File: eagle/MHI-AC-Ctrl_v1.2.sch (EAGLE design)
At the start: 15 parts, among them U1 TSR_1-2450

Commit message: - refactored board
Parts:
- removed TP6, TP7, TP8: TPPAD1-13, testpad:TPPAD1-13
- added R1: 4.7K, rcl:R-EU_0204/7
- added U2: DS18B20, DS18B20:DS18B20
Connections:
- net MISO_LV renamed N$1
- net MOSI_LV renamed N$2
- net +5V: now also R1.2, U2.VDD; no longer TP8.TP
- net GND: now also U2.GND; no longer TP7.TP
- net N$14: now also R1.1, U2.DQ; no longer TP6.TP
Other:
- note added: "Optional: DS18B20"
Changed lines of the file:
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@@
 <part name="P+2" library="supply1" library_urn="urn:adsk.eagle:library:371" deviceset="+5V" device=""/>
 <part name="P+3" library="supply1" library_urn="urn:adsk.eagle:library:371" deviceset="+12V" device=""/>
-<part name="GND5" library="supply1" library_urn="urn:adsk.eagle:library:371" deviceset="GND" device=""/>
 <part name="U$4" library="srg" deviceset="JST-PH_5-PIN_HEADER" device=""/>
 <part name="C2" library="rcl" library_urn="urn:adsk.eagle:library:334" deviceset="C-EU" device="025-024X044" package3d_urn="urn:adsk.eagle:package:23630/1" value="100n"/>
@@
 <part name="P+6" library="supply1" library_urn="urn:adsk.eagle:library:371" deviceset="+5V" device=""/>
 <part name="P+4" library="supply1" library_urn="urn:adsk.eagle:library:371" deviceset="+12V" device=""/>
-<part name="TP6" library="testpad" library_urn="urn:adsk.eagle:library:385" deviceset="TP" device="PAD1-13" package3d_urn="urn:adsk.eagle:package:27946/1"/>
-<part name="TP7" library="testpad" library_urn="urn:adsk.eagle:library:385" deviceset="TP" device="PAD1-13" package3d_urn="urn:adsk.eagle:package:27946/1"/>
-<part name="TP8" library="testpad" library_urn="urn:adsk.eagle:library:385" deviceset="TP" device="PAD1-13" package3d_urn="urn:adsk.eagle:package:27946/1"/>
-<part name="P+5" library="supply1" library_urn="urn:adsk.eagle:library:371" deviceset="+5V" device=""/>
 <part name="TP9" library="testpad" library_urn="urn:adsk.eagle:library:385" deviceset="TP" device="PAD1-13" package3d_urn="urn:adsk.eagle:package:27946/1"/>
 <part name="TP10" library="testpad" library_urn="urn:adsk.eagle:library:385" deviceset="TP" device="PAD1-13" package3d_urn="urn:adsk.eagle:package:27946/1"/>
@@
 <part name="TP12" library="testpad" library_urn="urn:adsk.eagle:library:385" deviceset="TP" device="PAD1-13" package3d_urn="urn:adsk.eagle:package:27946/1"/>
 <part name="TP13" library="testpad" library_urn="urn:adsk.eagle:library:385" deviceset="TP" device="PAD1-13" package3d_urn="urn:adsk.eagle:package:27946/1"/>
+<part name="R1" library="rcl" library_urn="urn:adsk.eagle:library:334" deviceset="R-EU_" device="0204/7" package3d_urn="urn:adsk.eagle:package:23498/2" value="4.7K"/>
+<part name="U2" library="DS18B20" deviceset="DS18B20" device=""/>
 </parts>
 <sheets>
 <sheet>
 <plain>
+<circle x="35.56" y="83.82" radius="23.417640625" width="0.1524" layer="94"/>
+<text x="25.4" y="101.6" size="1.778" layer="94">Optional: DS18B20</text>
 </plain>
 <instances>
@@
 <attribute name="VALUE" x="-27.94" y="76.2" size="1.778" layer="96"/>
 </instance>
-<instance part="GND5" gate="1" x="-30.48" y="30.48" smashed="yes">
-<attribute name="VALUE" x="-33.02" y="27.94" size="1.778" layer="96"/>
-</instance>
 <instance part="U$4" gate="G$1" x="-86.36" y="38.1" smashed="yes" rot="R180"/>
 <instance part="C2" gate="G$1" x="55.88" y="25.4" smashed="yes">
@@
 <attribute name="VALUE" x="11.684" y="61.341" size="1.778" layer="96"/>
 </instance>
-<instance part="GND9" gate="1" x="10.16" y="30.48" smashed="yes">
-<attribute name="VALUE" x="7.62" y="27.94" size="1.778" layer="96"/>
+<instance part="GND9" gate="1" x="-10.16" y="25.4" smashed="yes">
+<attribute name="VALUE" x="-12.7" y="22.86" size="1.778" layer="96"/>
 </instance>
 <instance part="LS1" gate="G$1" x="-10.16" y="43.18" smashed="yes" rot="MR0">
@@
 <attribute name="VALUE" x="-40.64" y="29.21" size="1.778" layer="96"/>
 </instance>
-<instance part="TP6" gate="G$1" x="60.96" y="35.56" smashed="yes" rot="R270">
-<attribute name="TP_SIGNAL_NAME" x="59.69" y="34.29" size="1.778" layer="97" rot="R270"/>
-</instance>
-<instance part="TP7" gate="G$1" x="68.58" y="36.83" smashed="yes">
-<attribute name="TP_SIGNAL_NAME" x="69.85" y="35.56" size="1.778" layer="97"/>
-</instance>
-<instance part="TP8" gate="G$1" x="68.58" y="45.72" smashed="yes" rot="R180">
-<attribute name="TP_SIGNAL_NAME" x="67.31" y="46.99" size="1.778" layer="97" rot="R180"/>
-</instance>
-<instance part="P+5" gate="1" x="68.58" y="52.07" smashed="yes">
-<attribute name="VALUE" x="71.12" y="54.61" size="1.778" layer="96" rot="R180"/>
-</instance>
 <instance part="TP9" gate="G$1" x="-55.88" y="49.53" smashed="yes">
 <attribute name="TP_SIGNAL_NAME" x="-54.61" y="48.26" size="1.778" layer="97"/>
@@
 <instance part="TP13" gate="G$1" x="-66.04" y="49.53" smashed="yes">
 <attribute name="TP_SIGNAL_NAME" x="-64.77" y="48.26" size="1.778" layer="97"/>
+</instance>
+<instance part="R1" gate="G$1" x="35.56" y="68.58" smashed="yes" rot="MR0">
+<attribute name="NAME" x="34.29" y="70.0786" size="1.778" layer="95" rot="MR0"/>
+<attribute name="VALUE" x="36.83" y="65.278" size="1.778" layer="96" rot="MR0"/>
+</instance>
+<instance part="U2" gate="G$1" x="35.56" y="88.9" smashed="yes" rot="MR0">
+<attribute name="NAME" x="43.194490625" y="96.78896875" size="1.78138125" layer="95" rot="MR0"/>
+<attribute name="VALUE" x="43.183340625" y="81.02255" size="1.77878125" layer="96" rot="MR0" align="top-left"/>
 </instance>
 </instances>
@@
 <pinref part="GND2" gate="1" pin="GND"/>
 <wire x1="55.88" y1="33.02" x2="68.58" y2="33.02" width="0.1524" layer="91"/>
-<pinref part="TP7" gate="G$1" pin="TP"/>
-<wire x1="68.58" y1="33.02" x2="68.58" y2="34.29" width="0.1524" layer="91"/>
-<junction x="68.58" y="33.02"/>
 </segment>
 <segment>
@@
 <wire x1="-78.74" y1="43.18" x2="-55.88" y2="43.18" width="0.1524" layer="91"/>
 <wire x1="-55.88" y1="43.18" x2="-30.48" y2="43.18" width="0.1524" layer="91"/>
-<pinref part="GND5" gate="1" pin="GND"/>
 <pinref part="LS1" gate="G$1" pin="GND.2"/>
-<wire x1="-30.48" y1="33.02" x2="-30.48" y2="40.64" width="0.1524" layer="91"/>
+<wire x1="-30.48" y1="27.94" x2="-30.48" y2="40.64" width="0.1524" layer="91"/>
 <wire x1="-30.48" y1="40.64" x2="-25.4" y2="40.64" width="0.1524" layer="91"/>
 <wire x1="-30.48" y1="43.18" x2="-30.48" y2="40.64" width="0.1524" layer="91"/>
@@
 <wire x1="-55.88" y1="43.18" x2="-55.88" y2="46.99" width="0.1524" layer="91"/>
 <junction x="-55.88" y="43.18"/>
+<pinref part="GND9" gate="1" pin="GND"/>
+<wire x1="7.62" y1="27.94" x2="-10.16" y2="27.94" width="0.1524" layer="91"/>
+<wire x1="-30.48" y1="27.94" x2="-10.16" y2="27.94" width="0.1524" layer="91"/>
+<junction x="-10.16" y="27.94"/>
+<pinref part="LS1" gate="G$1" pin="GND.1"/>
+<wire x1="5.08" y1="40.64" x2="7.62" y2="40.64" width="0.1524" layer="91"/>
+<wire x1="7.62" y1="40.64" x2="7.62" y2="27.94" width="0.1524" layer="91"/>
 </segment>
 <segment>
@@
 <junction x="-10.16" y="60.96"/>
 <wire x1="10.16" y1="60.96" x2="-10.16" y2="60.96" width="0.1524" layer="91"/>
-</segment>
-<segment>
-<pinref part="LS1" gate="G$1" pin="GND.1"/>
-<pinref part="GND9" gate="1" pin="GND"/>
-<wire x1="5.08" y1="40.64" x2="10.16" y2="40.64" width="0.1524" layer="91"/>
-<wire x1="10.16" y1="40.64" x2="10.16" y2="33.02" width="0.1524" layer="91"/>
+<pinref part="U2" gate="G$1" pin="GND"/>
+<wire x1="25.4" y1="83.82" x2="25.4" y2="60.96" width="0.1524" layer="91"/>
+<wire x1="25.4" y1="60.96" x2="10.16" y2="60.96" width="0.1524" layer="91"/>
+<junction x="10.16" y="60.96"/>
 </segment>
 </net>
@@
 <wire x1="0" y1="68.58" x2="10.16" y2="68.58" width="0.1524" layer="91"/>
 <junction x="10.16" y="68.58"/>
+<wire x1="10.16" y1="68.58" x2="20.32" y2="68.58" width="0.1524" layer="91"/>
+<wire x1="20.32" y1="68.58" x2="20.32" y2="93.98" width="0.1524" layer="91"/>
+<pinref part="U2" gate="G$1" pin="VDD"/>
+<wire x1="20.32" y1="93.98" x2="25.4" y2="93.98" width="0.1524" layer="91"/>
+<pinref part="R1" gate="G$1" pin="2"/>
+<wire x1="20.32" y1="68.58" x2="30.48" y2="68.58" width="0.1524" layer="91"/>
+<junction x="20.32" y="68.58"/>
 </segment>
 <segment>
@@
 <pinref part="LS1" gate="G$1" pin="HV"/>
 <wire x1="-27.94" y1="43.18" x2="-25.4" y2="43.18" width="0.1524" layer="91"/>
-</segment>
-<segment>
-<pinref part="P+5" gate="1" pin="+5V"/>
-<pinref part="TP8" gate="G$1" pin="TP"/>
-<wire x1="68.58" y1="49.53" x2="68.58" y2="48.26" width="0.1524" layer="91"/>
 </segment>
 </net>
@@
 </segment>
 </net>
-<net name="MOSI_LV" class="0">
-<segment>
-<pinref part="U$1" gate="G$1" pin="D7"/>
-<pinref part="LS1" gate="G$1" pin="LV4"/>
-<wire x1="20.32" y1="35.56" x2="5.08" y2="35.56" width="0.1524" layer="91"/>
-</segment>
-</net>
-<net name="MISO_LV" class="0">
-<segment>
-<pinref part="U$1" gate="G$1" pin="D6"/>
-<pinref part="LS1" gate="G$1" pin="LV3"/>
-<wire x1="20.32" y1="38.1" x2="5.08" y2="38.1" width="0.1524" layer="91"/>
-</segment>
-</net>
 <net name="SCL_LV" class="0">
 <segment>
@@
 <segment>
 <pinref part="U$1" gate="G$1" pin="D4"/>
-<pinref part="TP6" gate="G$1" pin="TP"/>
 <wire x1="55.88" y1="35.56" x2="58.42" y2="35.56" width="0.1524" layer="91"/>
-</segment>
-</net>
+<wire x1="58.42" y1="35.56" x2="58.42" y2="68.58" width="0.1524" layer="91"/>
+<pinref part="U2" gate="G$1" pin="DQ"/>
+<pinref part="R1" gate="G$1" pin="1"/>
+<wire x1="45.72" y1="68.58" x2="45.72" y2="88.9" width="0.1524" layer="91"/>
+<wire x1="40.64" y1="68.58" x2="45.72" y2="68.58" width="0.1524" layer="91"/>
+<junction x="45.72" y="68.58"/>
+<wire x1="45.72" y1="68.58" x2="58.42" y2="68.58" width="0.1524" layer="91"/>
+</segment>
+</net>
+<net name="N$1" class="0">
+<segment>
+<pinref part="LS1" gate="G$1" pin="LV3"/>
+<pinref part="U$1" gate="G$1" pin="D6"/>
+<wire x1="5.08" y1="38.1" x2="20.32" y2="38.1" width="0.1524" layer="91"/>
+</segment>
+</net>
+<net name="N$2" class="0">
+<segment>
+<pinref part="LS1" gate="G$1" pin="LV4"/>
+<pinref part="U$1" gate="G$1" pin="D7"/>
+<wire x1="5.08" y1="35.56" x2="20.32" y2="35.56" width="0.1524" layer="91"/>
+</segment>
+</net>

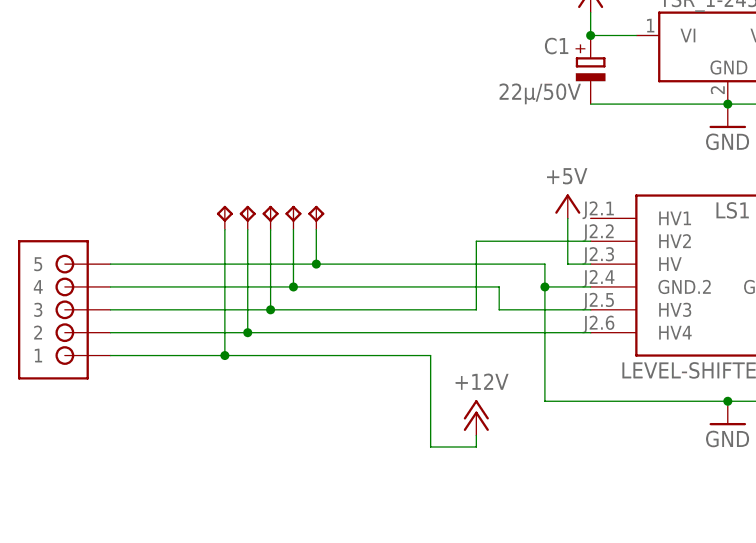
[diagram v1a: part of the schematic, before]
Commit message: invert pin 2 and 3, remove AIRWIRE from DS18x20
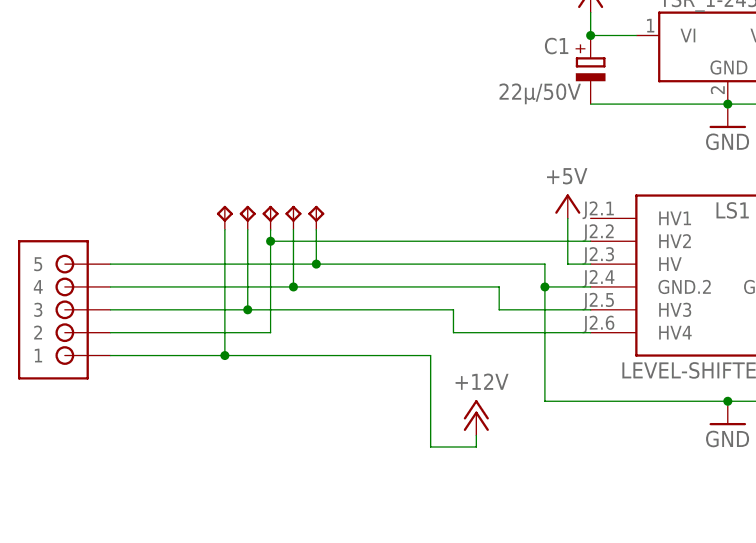
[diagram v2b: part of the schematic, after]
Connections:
- removed net MOSI: LS1.HV4, TP12.TP, U$4.2
- removed net SCL: LS1.HV2, TP11.TP, U$4.3
- new net N$3: LS1.HV2, TP11.TP, U$4.2
- new net N$4: LS1.HV4, TP12.TP, U$4.3
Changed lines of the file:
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@@
-</segment>
-</net>
-<net name="MOSI" class="0">
-<segment>
-<wire x1="-25.4" y1="35.56" x2="-63.5" y2="35.56" width="0.1524" layer="91"/>
-<pinref part="LS1" gate="G$1" pin="HV4"/>
-<wire x1="-63.5" y1="35.56" x2="-63.5" y2="46.99" width="0.1524" layer="91"/>
-<pinref part="TP12" gate="G$1" pin="TP"/>
-<pinref part="U$4" gate="G$1" pin="2"/>
-<wire x1="-63.5" y1="35.56" x2="-78.74" y2="35.56" width="0.1524" layer="91"/>
-<junction x="-63.5" y="35.56"/>
 </segment>
 </net>
@@
 </segment>
 </net>
-<net name="SCL" class="0">
-<segment>
-<wire x1="-38.1" y1="45.72" x2="-38.1" y2="38.1" width="0.1524" layer="91"/>
-<pinref part="U$4" gate="G$1" pin="3"/>
-<wire x1="-38.1" y1="38.1" x2="-60.96" y2="38.1" width="0.1524" layer="91"/>
-<pinref part="LS1" gate="G$1" pin="HV2"/>
-<wire x1="-60.96" y1="38.1" x2="-78.74" y2="38.1" width="0.1524" layer="91"/>
-<wire x1="-38.1" y1="45.72" x2="-25.4" y2="45.72" width="0.1524" layer="91"/>
-<pinref part="TP11" gate="G$1" pin="TP"/>
-<wire x1="-60.96" y1="38.1" x2="-60.96" y2="46.99" width="0.1524" layer="91"/>
-<junction x="-60.96" y="38.1"/>
-</segment>
-</net>
 <net name="N$14" class="0">
 <segment>
@@
 </segment>
 </net>
+<net name="N$3" class="0">
+<segment>
+<pinref part="TP11" gate="G$1" pin="TP"/>
+<pinref part="LS1" gate="G$1" pin="HV2"/>
+<wire x1="-25.4" y1="45.72" x2="-60.96" y2="45.72" width="0.1524" layer="91"/>
+<wire x1="-60.96" y1="45.72" x2="-60.96" y2="46.99" width="0.1524" layer="91"/>
+<junction x="-60.96" y="45.72"/>
+<pinref part="U$4" gate="G$1" pin="2"/>
+<wire x1="-60.96" y1="35.56" x2="-60.96" y2="45.72" width="0.1524" layer="91"/>
+<wire x1="-78.74" y1="35.56" x2="-60.96" y2="35.56" width="0.1524" layer="91"/>
+</segment>
+</net>
+<net name="N$4" class="0">
+<segment>
+<pinref part="U$4" gate="G$1" pin="3"/>
+<wire x1="-78.74" y1="38.1" x2="-63.5" y2="38.1" width="0.1524" layer="91"/>
+<wire x1="-63.5" y1="38.1" x2="-40.64" y2="38.1" width="0.1524" layer="91"/>
+<wire x1="-40.64" y1="38.1" x2="-40.64" y2="35.56" width="0.1524" layer="91"/>
+<pinref part="LS1" gate="G$1" pin="HV4"/>
+<wire x1="-40.64" y1="35.56" x2="-25.4" y2="35.56" width="0.1524" layer="91"/>
+<pinref part="TP12" gate="G$1" pin="TP"/>
+<wire x1="-63.5" y1="46.99" x2="-63.5" y2="38.1" width="0.1524" layer="91"/>
+<junction x="-63.5" y="38.1"/>
+</segment>
+</net>
